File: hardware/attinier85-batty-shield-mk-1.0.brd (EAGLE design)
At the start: 36 x 25 mm, 6 parts, among them U1 ATTINIEST85_SHIELDV2

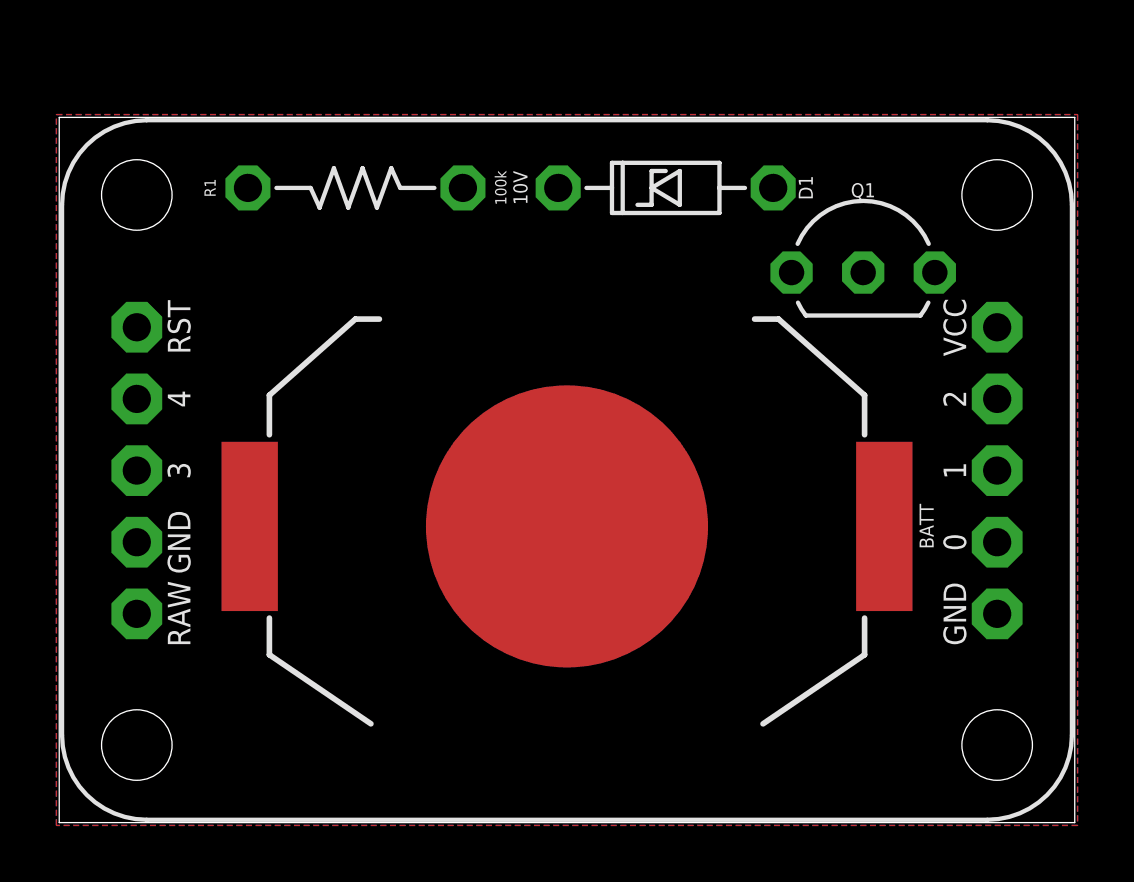
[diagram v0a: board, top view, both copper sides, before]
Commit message: renaming parts
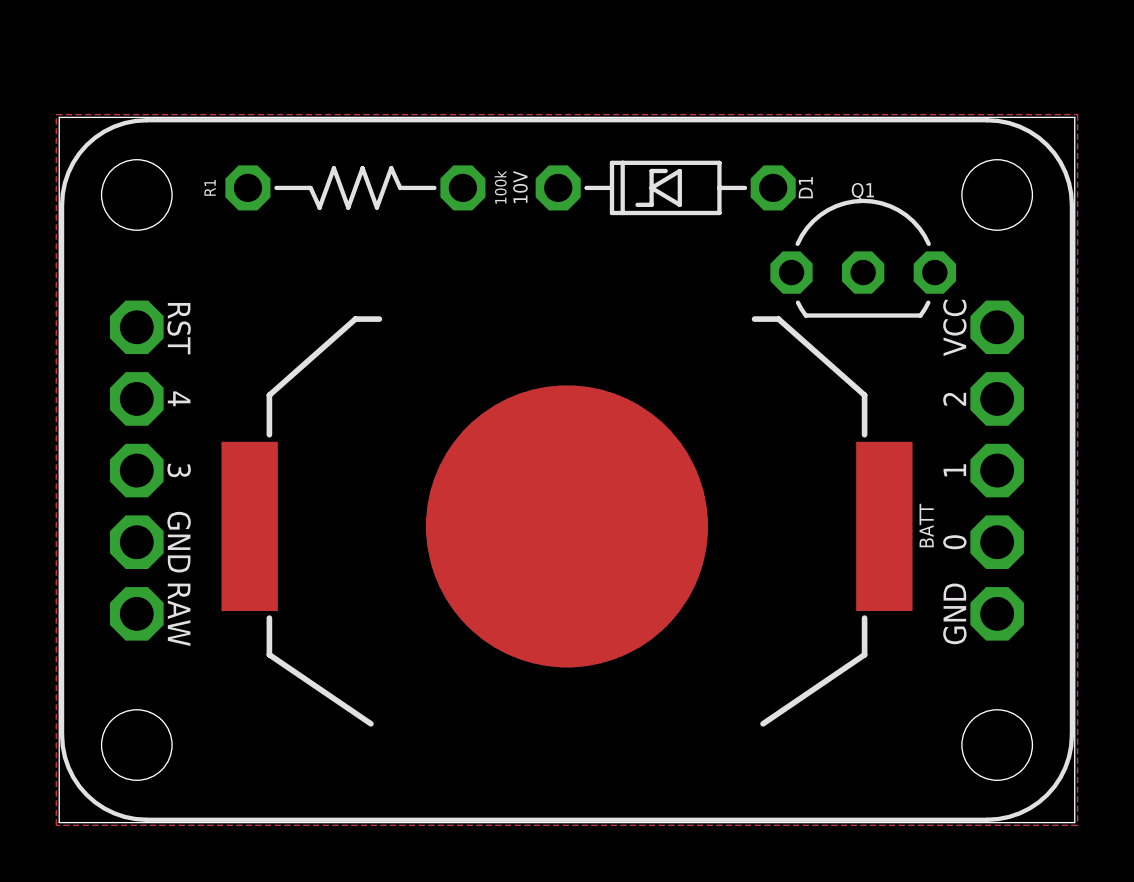
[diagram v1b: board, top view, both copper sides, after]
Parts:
- U1: value ATTINIEST85_SHIELDV2 -> ATTINIER85_SHIELDV2; device A_butts:ATTINIEST85_SHIELD_V2 -> A_butts:ATTINIER85_SHIELD_V2
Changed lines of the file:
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@@
 <attribute name="DESIGNER" value="Nobody" x="13.97" y="-1.27" size="1.778" layer="27" display="off"/>
 </element>
-<element name="U1" library="A_butts" package="ATTINIEST85_SHIELD_V2" value="ATTINIEST85_SHIELDV2" x="18" y="12.5"/>
+<element name="U1" library="A_butts" package="ATTINIER85_SHIELD_V2" value="ATTINIER85_SHIELDV2" x="18" y="12.5"/>
 <element name="BATT" library="A_butts" package="BATTCON_20MM_MINE" value="CR2032" x="18" y="10.5" rot="R270"/>
 <element name="D1" library="A_butts" package="DIODE-ZENNER-7.62MM" value="10V" x="21.5" y="22.5" rot="R180"/>

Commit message: cleaning up version spoo
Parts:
- removed D1: 10V, A_butts:DIODE-ZENNER-7.62MM
- removed Q1: (no value), A_butts:TO-92-AMMO
- removed R1: 100k, A_butts:RESISTOR-AXIAL-PTH-7.62MM
- added JP1: VCC RAW, A_butts:PAD-JUMPER-3-NO_YES_SILK_FULL_BOX
- added PWR: SWITCH-SPDTPTH-RA-2MM, A_butts:SPDT-RA-2MM
- added U$3: (no value), A_butts:CC-BY-SA-4.0-NO-URL
- added U$4: (no value), A_butts:OSHWLOGO_TOP_0.2
- added U$6: (no value), A_butts:COW_METAL
- moved BATT 0.10 mm to (18.0, 10.4)
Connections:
- removed net N$1: D1.K, Q1.2, R1.P$2
- removed net V_BATT: BATT.TOP@1, D1.A, Q1.1
- new net RAW: JP1.1, U1.RAW
- new net VBATT: BATT.TOP@1, BATT.TOP@2, PWR.2
- net GND: now also U1.GND@1; no longer R1.P$1
- net VCC: now also JP1.2, JP1.3, PWR.1; no longer Q1.3
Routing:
- net VBATT: track 0.00 -> 38.2 mm
- net RAW: track 0.00 -> 36.8 mm
- net VCC: track 0.00 -> 16.5 mm
- removed copper zone on layer 16, net GND
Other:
- outline, holes or cut-outs redrawn
- board text added: "+ side goes up"
- board text added: ">AUTHOR"
- board text added: ">VERSION"
- board text added: "ATTinier85 Batty Shield"
- board text added: "CR2032"
- board text added: "OFF"
- board text added: "ON"
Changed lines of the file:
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@@
 <layer number="27" name="tValues" color="7" fill="1" visible="yes" active="yes"/>
 <layer number="28" name="bValues" color="7" fill="1" visible="yes" active="yes"/>
-<layer number="29" name="tStop" color="7" fill="3" visible="no" active="yes"/>
-<layer number="30" name="bStop" color="7" fill="6" visible="no" active="yes"/>
+<layer number="29" name="tStop" color="7" fill="3" visible="yes" active="yes"/>
+<layer number="30" name="bStop" color="7" fill="6" visible="yes" active="yes"/>
 <layer number="31" name="tCream" color="7" fill="4" visible="no" active="yes"/>
 <layer number="32" name="bCream" color="7" fill="5" visible="no" active="yes"/>
@@
 <board>
 <plain>
-<wire x1="0" y1="0" x2="36" y2="0" width="0" layer="20"/>
-<wire x1="36" y1="0" x2="36" y2="25" width="0" layer="20"/>
-<wire x1="36" y1="25" x2="0" y2="25" width="0" layer="20"/>
-<wire x1="0" y1="25" x2="0" y2="0" width="0" layer="20"/>
+<wire x1="0" y1="22" x2="0" y2="3" width="0" layer="20"/>
+<wire x1="0" y1="3" x2="3" y2="0" width="0" layer="20" curve="90"/>
+<wire x1="3" y1="0" x2="33" y2="0" width="0" layer="20"/>
+<wire x1="33" y1="0" x2="36" y2="3" width="0" layer="20" curve="90"/>
+<wire x1="36" y1="3" x2="36" y2="22" width="0" layer="20"/>
+<wire x1="36" y1="22" x2="33" y2="25" width="0" layer="20" curve="90"/>
+<wire x1="33" y1="25" x2="3" y2="25" width="0" layer="20"/>
+<wire x1="3" y1="25" x2="0" y2="22" width="0" layer="20" curve="90"/>
+<text x="12.5" y="22.75" size="1" layer="21" font="vector" ratio="16" rot="SR270" align="top-center">ON</text>
+<text x="23.5" y="22.75" size="1" layer="21" font="vector" ratio="16" rot="SR90" align="top-center">OFF</text>
+<text x="28.3" y="2.6" size="1" layer="21" font="vector" ratio="16" align="center">+ side
+goes up</text>
+<text x="18" y="6" size="1.5" layer="22" font="vector" ratio="15" rot="MR0" align="top-center">ATTinier85 Batty Shield</text>
+<text x="18" y="4" size="1" layer="22" font="vector" ratio="16" rot="MR0" align="top-center">&gt;VERSION</text>
+<text x="18" y="2.5" size="1" layer="22" font="vector" ratio="16" rot="MR0" align="top-center">&gt;AUTHOR</text>
+<text x="18" y="6" size="1.5" layer="16" font="vector" ratio="15" rot="MR0" align="top-center">ATTinier85 Batty Shield</text>
+<text x="8" y="23" size="1" layer="21" font="vector" ratio="16" align="center">&gt;VERSION</text>
+<text x="8" y="23" size="1" layer="1" font="vector" ratio="16" align="center">&gt;VERSION</text>
+<text x="28.3" y="2.6" size="1" layer="1" font="vector" ratio="16" align="center">+ side
+goes up</text>
+<text x="18" y="2.5" size="1" layer="16" font="vector" ratio="16" rot="MR0" align="top-center">&gt;AUTHOR</text>
+<text x="18" y="4" size="1" layer="16" font="vector" ratio="16" rot="MR0" align="top-center">&gt;VERSION</text>
+<text x="8" y="2.5" size="1" layer="21" font="vector" ratio="16" align="center">CR2032</text>
+<text x="8" y="2.5" size="1" layer="1" font="vector" ratio="16" align="center">CR2032</text>
 </plain>
 <attributes>
+<attribute name="AUTHOR" value="by schizobovine &lt;sean@yak.net&gt;"/>
+<attribute name="VERSION" value="Rev 1.0"/>
 </attributes>
 <variantdefs>
@@
 </element>
 <element name="U1" library="A_butts" package="ATTINIER85_SHIELD_V2" value="ATTINIER85_SHIELDV2" x="18" y="12.5"/>
-<element name="BATT" library="A_butts" package="BATTCON_20MM_MINE" value="CR2032" x="18" y="10.5" rot="R270"/>
-<element name="D1" library="A_butts" package="DIODE-ZENNER-7.62MM" value="10V" x="21.5" y="22.5" rot="R180"/>
-<element name="R1" library="A_butts" package="RESISTOR-AXIAL-PTH-7.62MM" value="100k" x="10.5" y="22.5"/>
-<element name="Q1" library="A_butts" package="TO-92-AMMO" value="" x="28.5" y="19.5"/>
+<element name="BATT" library="A_butts" package="BATTCON_20MM_MINE" value="CR2032" x="18" y="10.4" smashed="yes" rot="R270"/>
+<element name="U$3" library="A_butts" package="CC-BY-SA-4.0-NO-URL" value="" x="27.5" y="12.5" rot="MR0"/>
+<element name="U$4" library="A_butts" package="OSHWLOGO_TOP_0.2" value="" x="8.5" y="12.5" rot="MR0"/>
+<element name="U$6" library="A_butts" package="COW_METAL" value="" x="18" y="12.5" rot="MR0"/>
+<element name="PWR" library="A_butts" package="SPDT-RA-2MM" value="SWITCH-SPDTPTH-RA-2MM" x="18" y="22.45" smashed="yes" rot="R180"/>
+<element name="JP1" library="A_butts" package="PAD-JUMPER-3-NO_YES_SILK_FULL_BOX" value="VCC   RAW" x="29" y="21.5" smashed="yes" rot="R270">
+<attribute name="NAME" x="30.25" y="21.5" size="0.8" layer="25" font="vector" ratio="12" rot="R270" align="bottom-center"/>
+<attribute name="VALUE" x="27.75" y="21.5" size="0.6" layer="21" font="vector" ratio="12" rot="R270" align="top-center"/>
+</element>
 </elements>
 <signals>
@@
 <vertex x="36.1" y="-0.1"/>
 </polygon>
-<polygon width="0.1524" layer="16">
-<vertex x="-0.1" y="-0.1"/>
-<vertex x="-0.1" y="25.1"/>
-<vertex x="36.1" y="25.1"/>
-<vertex x="36.1" y="-0.1"/>
-</polygon>
 <contactref element="BATT" pad="BOTTOM"/>
-<contactref element="R1" pad="P$1"/>
 <contactref element="U1" pad="GND@2"/>
+<contactref element="U1" pad="GND@1"/>
 </signal>
-<signal name="V_BATT">
-<contactref element="Q1" pad="1"/>
-<contactref element="D1" pad="A"/>
+<signal name="VBATT">
+<contactref element="BATT" pad="TOP@2"/>
 <contactref element="BATT" pad="TOP@1"/>
-<wire x1="25.31" y1="22.5" x2="25.96" y2="19.5" width="0" layer="19" extent="1-1"/>
-<wire x1="29.25" y1="10.5" x2="25.96" y2="19.5" width="0" layer="19" extent="1-1"/>
+<contactref element="PWR" pad="2"/>
+<wire x1="6.75" y1="10.4" x2="6.75" y2="15" width="0.5" layer="1"/>
+<wire x1="6.75" y1="15" x2="12.65" y2="20.9" width="0.5" layer="1"/>
+<wire x1="12.65" y1="20.9" x2="18" y2="20.9" width="0.5" layer="1"/>
+<wire x1="18" y1="20.9" x2="18" y2="22.45" width="0.5" layer="1"/>
+<wire x1="29.25" y1="10.4" x2="29.3" y2="10.45" width="0.5" layer="1"/>
+<wire x1="29.3" y1="10.45" x2="29.3" y2="15" width="0.5" layer="1"/>
+<wire x1="18" y1="20.9" x2="23.4" y2="20.9" width="0.5" layer="1"/>
+<wire x1="23.4" y1="20.9" x2="29.3" y2="15" width="0.5" layer="1"/>
+</signal>
+<signal name="RAW">
+<contactref element="U1" pad="RAW"/>
+<contactref element="JP1" pad="1"/>
+<wire x1="29" y1="23.024" x2="22.376" y2="23.024" width="0.5" layer="1"/>
+<wire x1="22.376" y1="23.024" x2="21.4" y2="24" width="0.5" layer="1"/>
+<wire x1="2.75" y1="7.4" x2="4.7" y2="9.35" width="0.5" layer="1"/>
+<wire x1="4.7" y1="9.35" x2="4.7" y2="15" width="0.5" layer="1"/>
+<wire x1="4.7" y1="15" x2="13.7" y2="24" width="0.5" layer="1"/>
+<wire x1="13.7" y1="24" x2="21.4" y2="24" width="0.5" layer="1"/>
 </signal>
 <signal name="VCC">
 <contactref element="U1" pad="VCC"/>
-<contactref element="Q1" pad="3"/>
-<wire x1="31.04" y1="19.5" x2="33.25" y2="17.56" width="0" layer="19" extent="1-1"/>
-</signal>
-<signal name="N$1">
-<contactref element="R1" pad="P$2"/>
-<contactref element="Q1" pad="2"/>
-<contactref element="D1" pad="K"/>
-<wire x1="17.69" y1="22.5" x2="28.5" y2="19.5" width="0" layer="19" extent="1-1"/>
-<wire x1="14.31" y1="22.5" x2="17.69" y2="22.5" width="0" layer="19" extent="1-1"/>
+<contactref element="JP1" pad="3"/>
+<contactref element="PWR" pad="1"/>
+<contactref element="JP1" pad="2"/>
+<wire x1="20.1" y1="22.45" x2="20.55" y2="22" width="0.5" layer="1"/>
+<wire x1="20.55" y1="22" x2="24" y2="22" width="0.5" layer="1"/>
+<wire x1="24" y1="22" x2="24.5" y2="21.5" width="0.5" layer="1"/>
+<wire x1="24.5" y1="21.5" x2="29" y2="21.5" width="0.5" layer="1"/>
+<wire x1="29" y1="21.5" x2="29" y2="19.976" width="0.5" layer="1"/>
+<wire x1="30.64" y1="17.56" x2="33.25" y2="17.56" width="0.5" layer="1"/>
+<wire x1="29" y1="19.976" x2="29" y2="19.2" width="0.5" layer="1"/>
+<wire x1="29" y1="19.2" x2="30.64" y2="17.56" width="0.5" layer="1"/>
 </signal>
 </signals>
 </board>
 </drawing>
+<compatibility>
+<note version="6.3" minversion="6.2.2" severity="warning">
+Since Version 6.2.2 text objects can contain more than one line,
+which will not be processed correctly with this version.
+</note>
+</compatibility>
 </eagle>
